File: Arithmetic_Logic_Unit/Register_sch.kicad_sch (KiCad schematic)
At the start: 2 parts, among them IC1 SN54173J, IC2 SN54173J

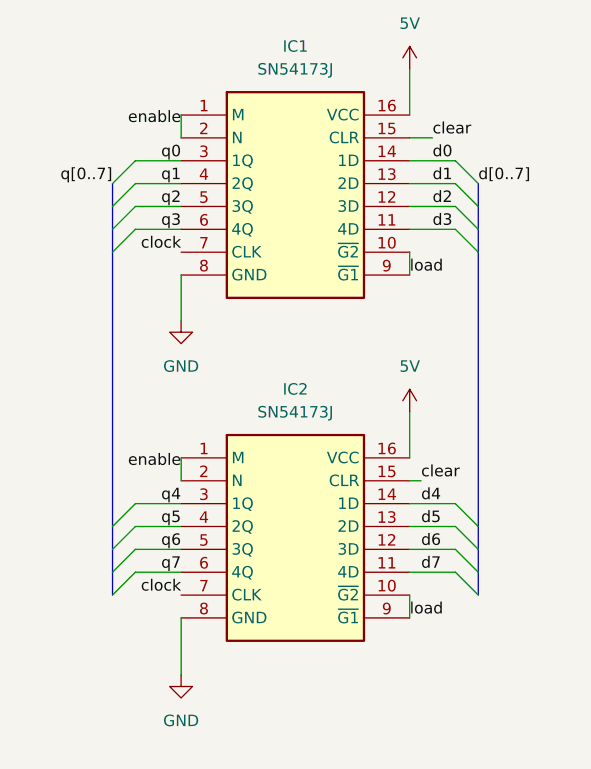
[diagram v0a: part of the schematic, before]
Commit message: updated wiki, created board outline for alu, made registers with hierarchical label
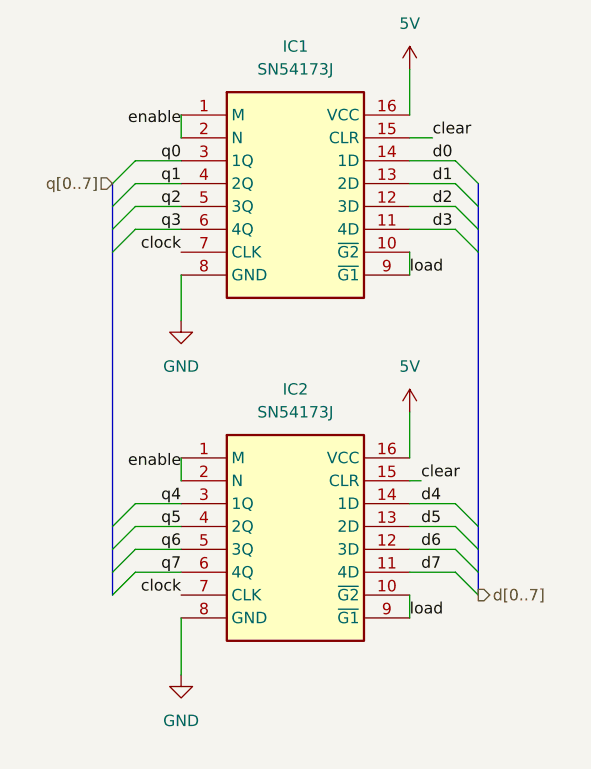
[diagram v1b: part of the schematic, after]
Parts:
- IC1, IC2: footprint CDIP762W66P254L2134H508Q16 -> footprints:SN54173J

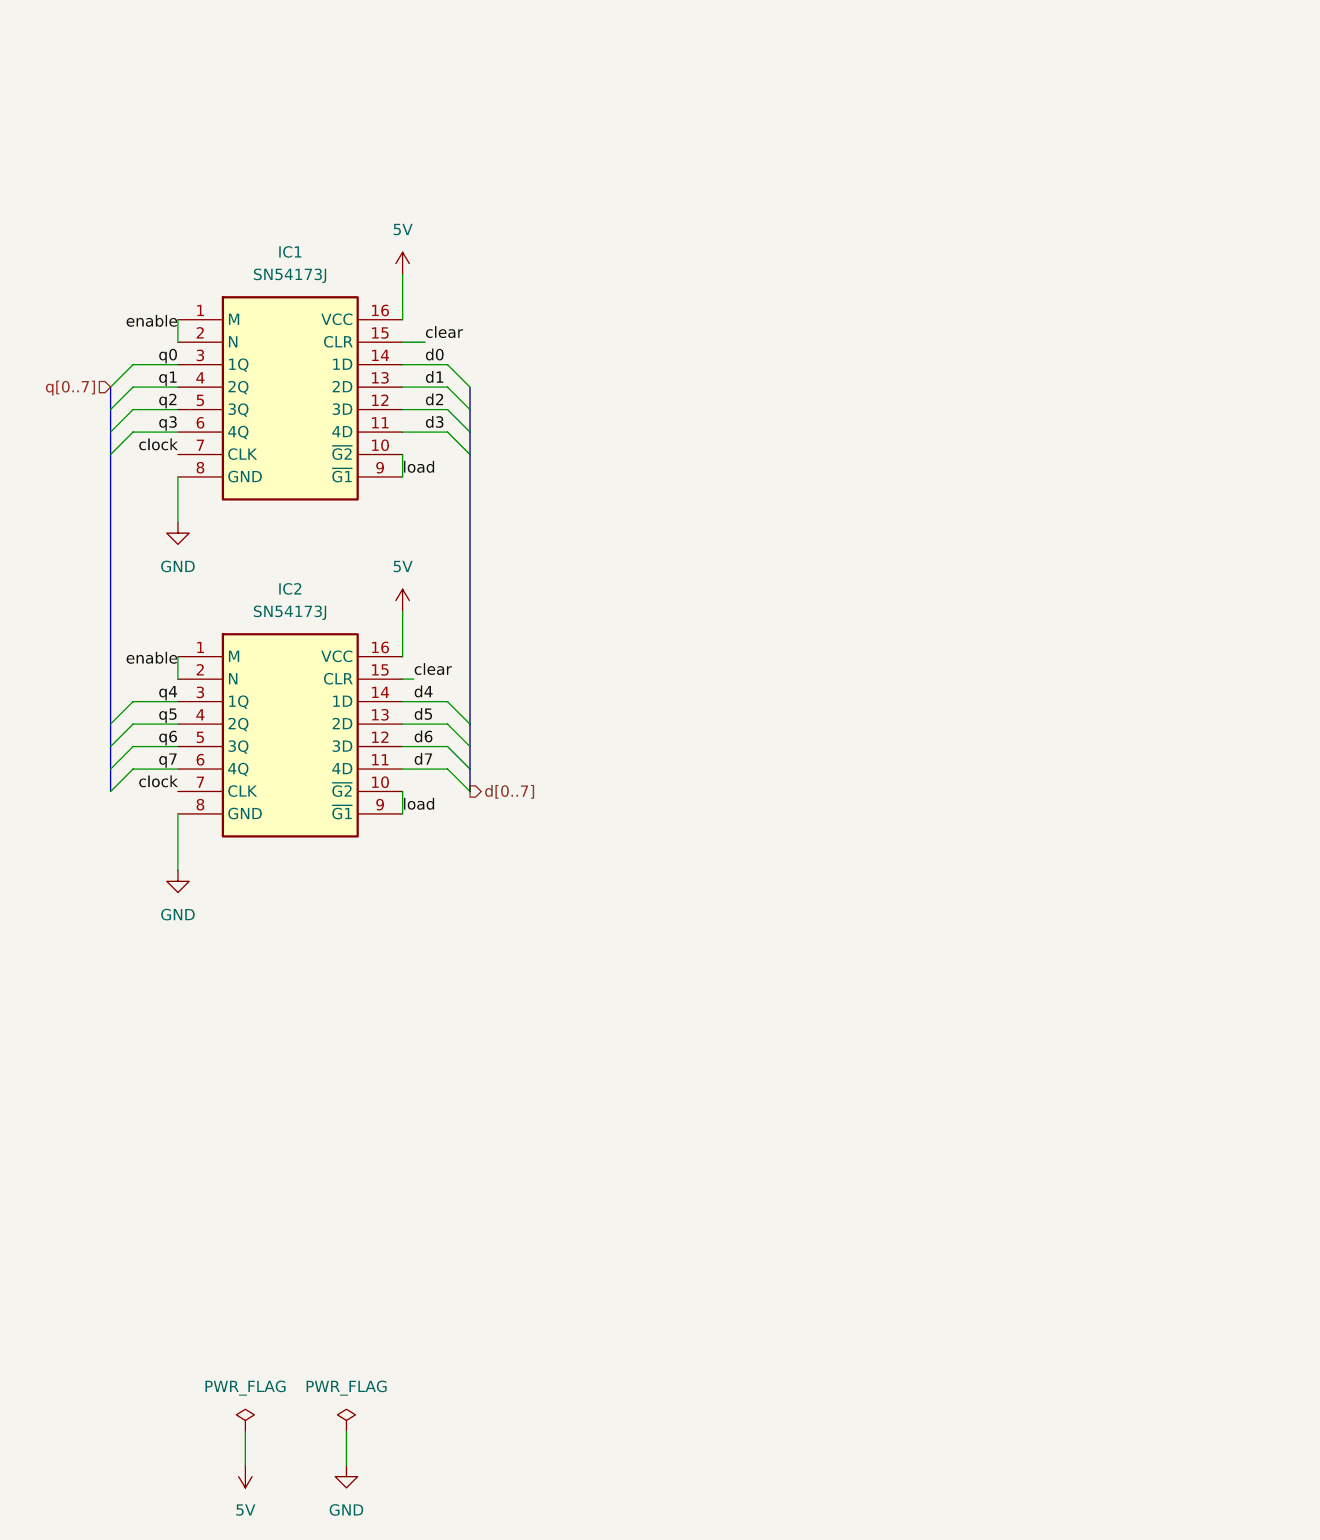
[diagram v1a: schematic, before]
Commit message: fixed register schematic
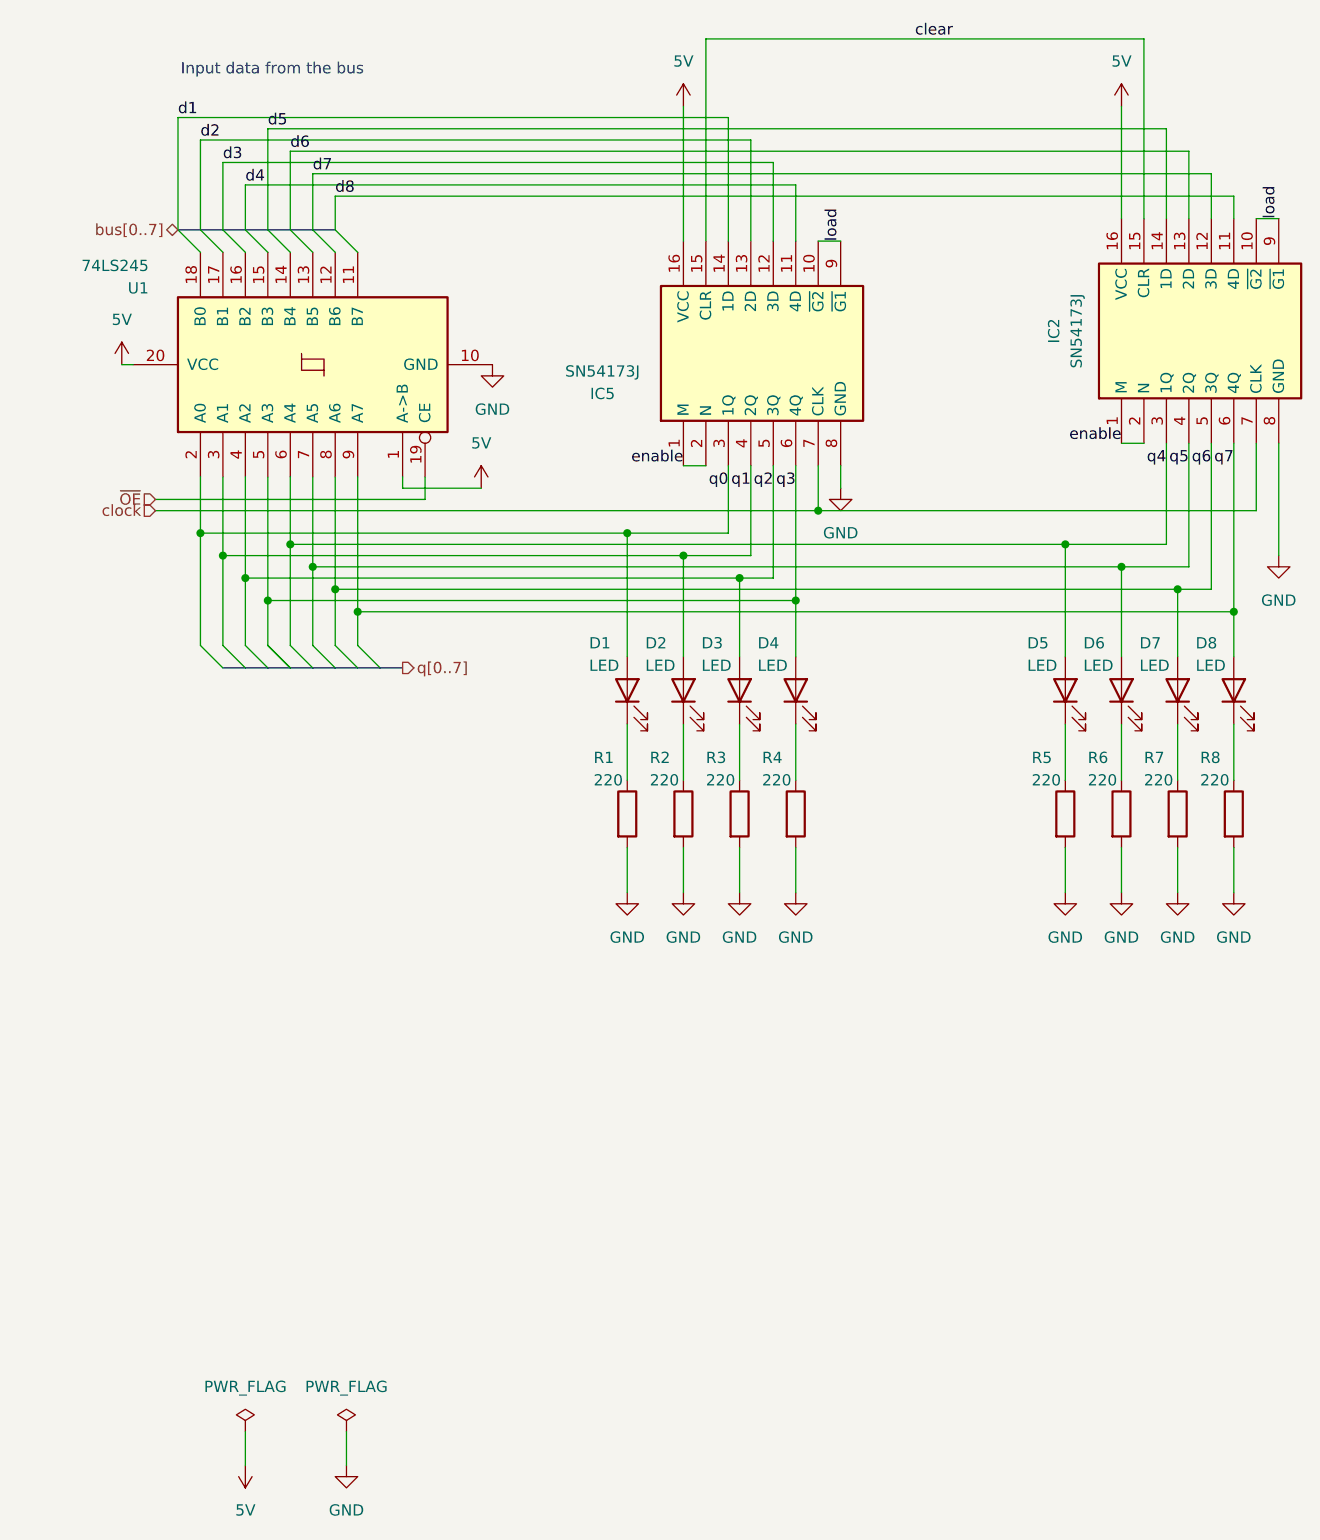
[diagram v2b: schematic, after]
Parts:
- added D1, D2, D3, D4, D5, D6, D7, D8: LED, symbol Device:LED
- added R1, R2, R3, R4, R5, R6, R7, R8: 220, symbol Device:R
- added U1: 74LS245, symbol 74xx:74LS245
- renumbered IC1 to IC5
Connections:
- net d1 is gone; now on net d2: IC5.13 (2D)
- net 5V: now also U1.1 (A->B), U1.20 (VCC)
- net GND: now also R1.2, R2.2, R3.2, R4.2, R5.2, R6.2, R7.2, R8.2, U1.10 (GND)
- net d2: no longer IC5.12 (3D)
- net d3: now also IC5.12 (3D); no longer IC5.11 (4D)
- net d4: now also IC5.11 (4D); no longer IC2.14 (1D)
- net d5: now also IC2.14 (1D); no longer IC2.13 (2D)
- net d6: now also IC2.13 (2D); no longer IC2.12 (3D)
- net d7: now also IC2.12 (3D); no longer IC2.11 (4D)
- net q0: now also D1.2 (A), U1.2 (A0)
- net q1: now also D2.2 (A), U1.3 (A1)
- net q2: now also D3.2 (A), U1.4 (A2)
- net q3: now also D4.2 (A), U1.5 (A3)
- net q4: now also D5.2 (A), U1.6 (A4)
- net q5: now also D6.2 (A), U1.7 (A5)
- net q6: now also D7.2 (A), U1.8 (A6)
- net q7: now also D8.2 (A), U1.9 (A7)
- net d0 renamed bus[0..7]
- new net: D6.1 (K), R6.1
- new net: D2.1 (K), R2.1
- new net: D5.1 (K), R5.1
- new net: D3.1 (K), R3.1
- new net: D4.1 (K), R4.1
- new net: D8.1 (K), R8.1
- new net: D7.1 (K), R7.1
- new net: D1.1 (K), R1.1
- new net d8: IC2.11 (4D)
- new net ~{OE}: U1.19 (CE)
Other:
- note added: "Input data from the bus"
- moved on the sheet: IC2, IC5

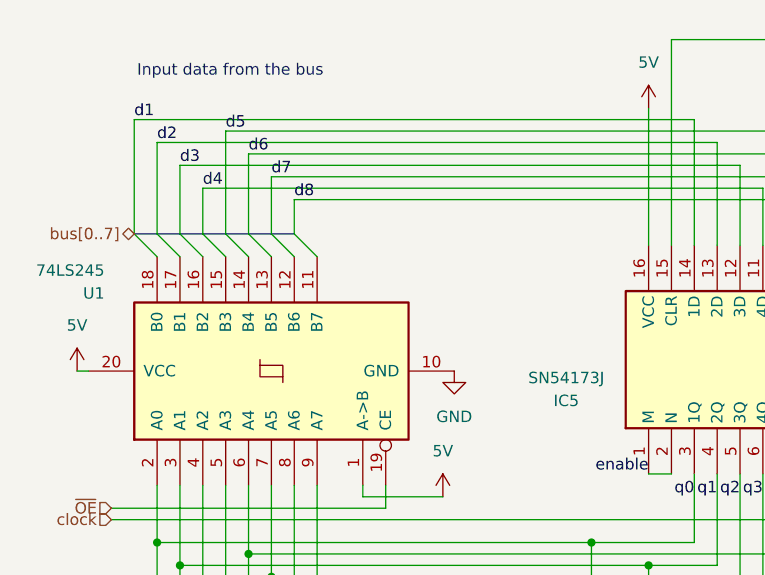
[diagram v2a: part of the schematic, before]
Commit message: completed alu schematic with errors
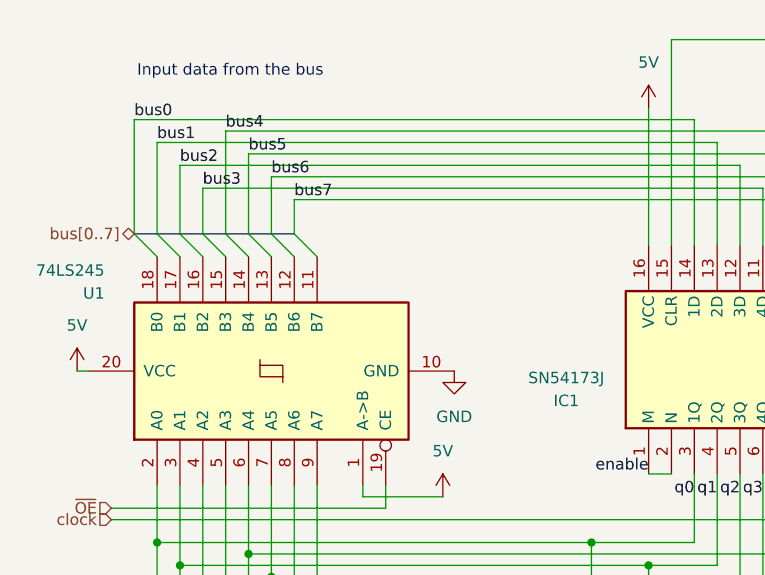
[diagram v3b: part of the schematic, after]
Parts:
- renumbered IC5 to IC1
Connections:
- net d2 renamed bus1
- net d3 renamed bus2
- net d4 renamed bus3
- net d5 renamed bus4
- net d6 renamed bus5
- net d7 renamed bus6
- net d8 renamed bus7
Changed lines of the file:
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@@
 			(width 0)
 			(type default)
+			(color 255 0 255 1)
 		)
 	)
@@
 			(width 0)
 			(type default)
+			(color 72 72 72 1)
 		)
 	)
@@
 			(width 0)
 			(type default)
+			(color 72 72 72 1)
 		)
 	)
@@
 			(width 0)
 			(type default)
+			(color 72 72 72 1)
 		)
 	)
@@
 		)
 	)
-	(label "d8"
+	(label "bus7"
 		(at 59.69 41.91 0)
 		(fields_autoplaced yes)
@@
 		)
 	)
-	(label "d6"
+	(label "bus5"
 		(at 54.61 36.83 0)
 		(fields_autoplaced yes)
@@
 		)
 	)
-	(label "d1"
+	(label "bus0"
 		(at 41.91 33.02 0)
 		(fields_autoplaced yes)
@@
 		)
 	)
-	(label "d5"
+	(label "bus4"
 		(at 52.07 34.29 0)
 		(fields_autoplaced yes)
@@
 		)
 	)
-	(label "d7"
+	(label "bus6"
 		(at 57.15 39.37 0)
 		(fields_autoplaced yes)
@@
 		)
 	)
-	(label "d4"
+	(label "bus3"
 		(at 49.53 40.64 0)
 		(fields_autoplaced yes)
@@
 		)
 	)
-	(label "d2"
+	(label "bus1"
 		(at 44.45 35.56 0)
 		(fields_autoplaced yes)
@@
 		)
 	)
-	(label "d3"
+	(label "bus2"
 		(at 46.99 38.1 0)
 		(fields_autoplaced yes)
@@
 		(on_board yes)
 		(dnp no)
-		(property "Reference" "IC5"
+		(property "Reference" "IC1"
 			(at 89.916 64.262 90)
 			(effects
